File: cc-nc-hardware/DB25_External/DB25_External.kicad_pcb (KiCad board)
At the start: 2 copper layers, 72.2 x 57.7 mm, 88 parts, among them J1 Conn_01x03_Male, J2 DB25_Male_MountingHoles, J4 SW, SW1 SW_MEC_5E, U1 SN74CBTD3384, U2 SN74CBTD3384, U3 AMS1117-2.85, U4 LVT245, U5 LVT125, U6 LVT125, U7 LVT125, U8 74HC14, U9 LVT245

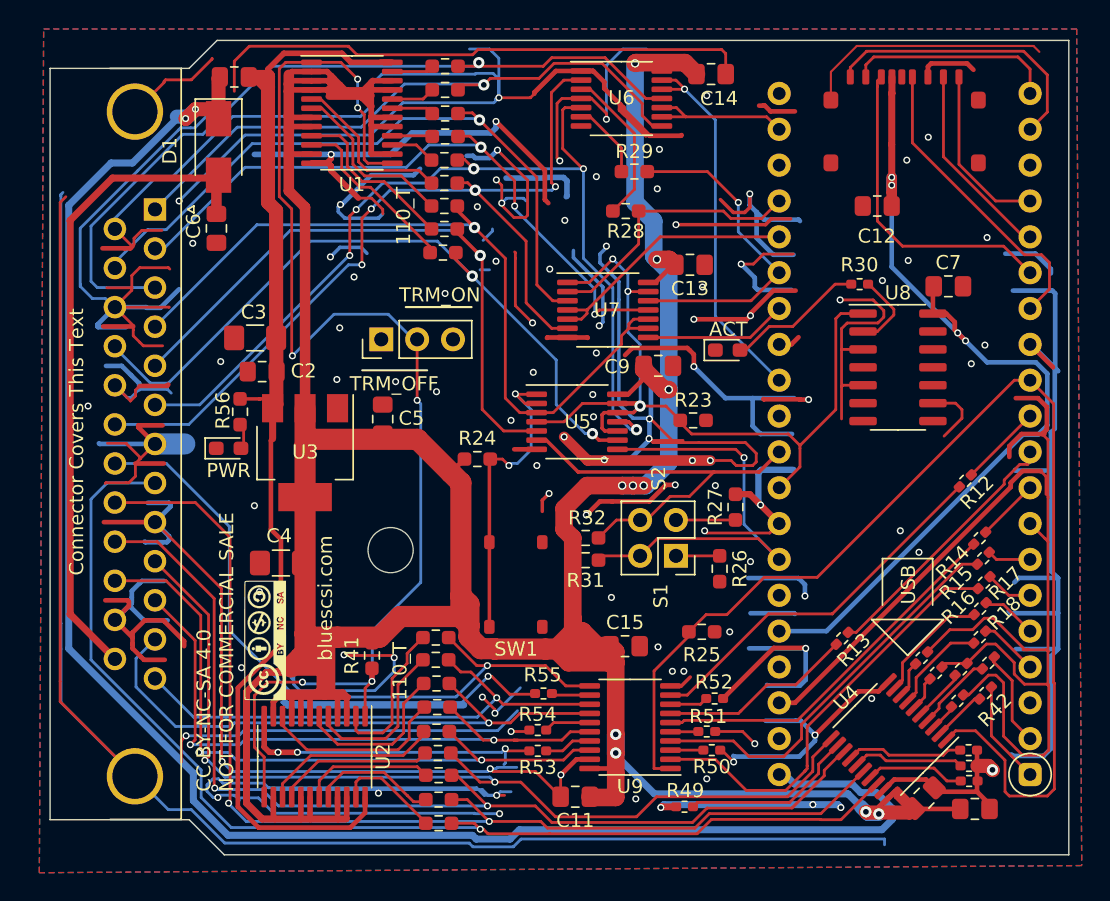
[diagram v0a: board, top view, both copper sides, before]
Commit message: DB25 2023_06a, Smaller Design
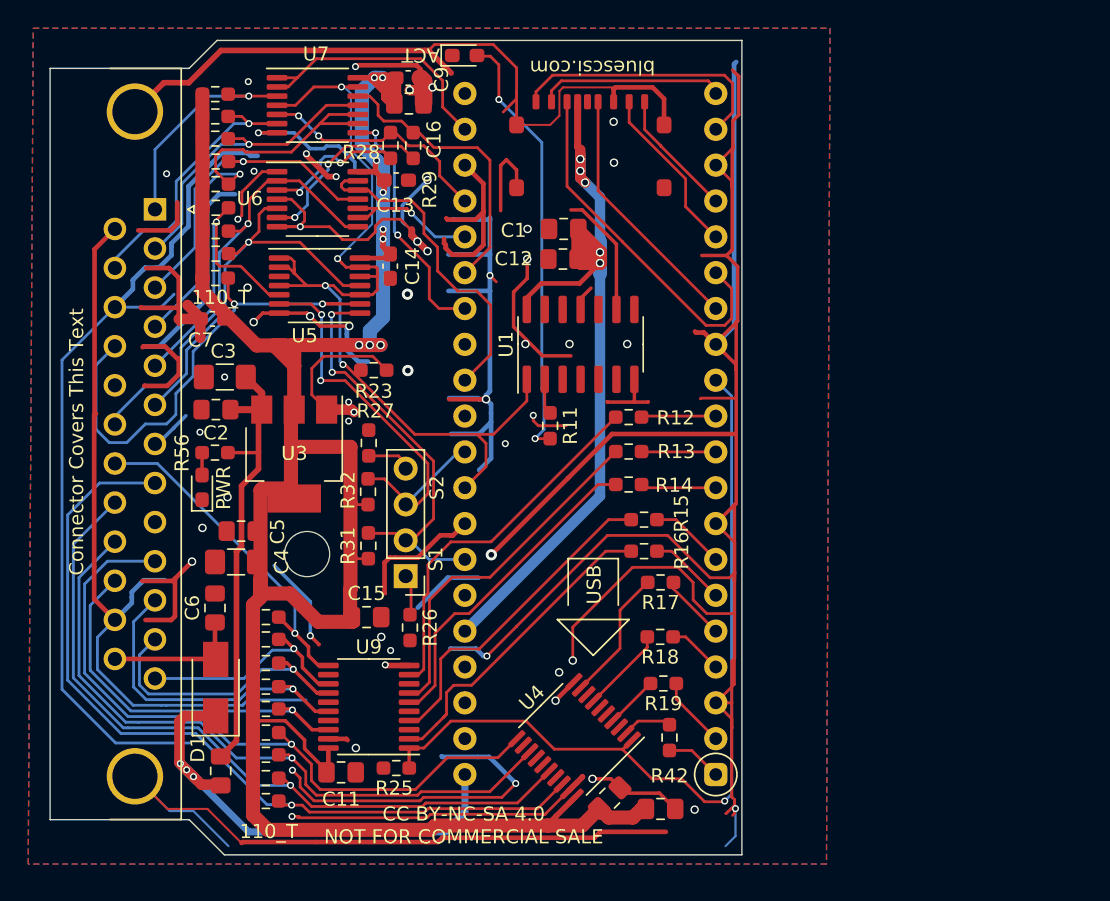
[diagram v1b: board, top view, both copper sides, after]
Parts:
- removed J4: SW, Connector_PinHeader_2.54mm:PinHeader_2x02_P2.54mm_Vertical
- removed R24: 1k, Resistor_SMD:R_0603_1608Metric_Pad0.98x0.95mm_HandSolder
- removed R30: 470, Resistor_SMD:R_0402_1005Metric_Pad0.72x0.64mm_HandSolder
- removed R41: 4.7k, Resistor_SMD:R_0603_1608Metric_Pad0.98x0.95mm_HandSolder
- removed R43, R44, R45, R46, R47, R48, R49, R50, R51, R52, R53, R54, R55: 1k, Resistor_SMD:R_0402_1005Metric_Pad0.72x0.64mm_HandSolder
- removed SW1: SW_MEC_5E, Library:TS-1187A-B-A-B
- removed U2: SN74CBTD3384, Package_SO:TSSOP-24_4.4x7.8mm_P0.65mm
- removed U8: 74HC14, Package_SO:SOIC-14_3.9x8.7mm_P1.27mm
- added C1: 100n, Capacitor_SMD:C_0805_2012Metric_Pad1.18x1.45mm_HandSolder, F.Cu at (136.4, 85.4)
- added C16: 4.7uF, Capacitor_SMD:C_0805_2012Metric_Pad1.18x1.45mm_HandSolder, F.Cu at (125.5, 76.6)
- C13, C14, C9: footprint Capacitor_SMD:C_0805_2012Metric_Pad1.18x1.45mm_HandSolder -> Capacitor_SMD:C_0603_1608Metric_Pad1.08x0.95mm_HandSolder
- C3, C4: value 20uF -> 47uF
- C7: value 4.7uF -> 0.1uF; footprint Capacitor_SMD:C_0805_2012Metric_Pad1.18x1.45mm_HandSolder -> Capacitor_SMD:C_0603_1608Metric_Pad1.08x0.95mm_HandSolder
- G***: moved to B.Cu
- J1: value Conn_01x03_Male -> Conn_01x04_Male; footprint Connector_PinHeader_2.54mm:PinHeader_1x03_P2.54mm_Vertical -> Connector_PinHeader_2.54mm:PinHeader_1x04_P2.54mm_Vertical
- R11: value 1k -> 470; footprint Resistor_SMD:R_0402_1005Metric_Pad0.72x0.64mm_HandSolder -> Resistor_SMD:R_0603_1608Metric_Pad0.98x0.95mm_HandSolder
- R12, R13, R14, R15, R16, R17, R18, R19, R42: footprint Resistor_SMD:R_0402_1005Metric_Pad0.72x0.64mm_HandSolder -> Resistor_SMD:R_0603_1608Metric_Pad0.98x0.95mm_HandSolder
- U1: value SN74CBTD3384 -> 74HC14; footprint Package_SO:TSSOP-24_4.4x7.8mm_P0.65mm -> Package_SO:SOIC-14_3.9x8.7mm_P1.27mm
- moved C7 52.2 mm to (111.5, 91.8), turned to 180 degrees
- moved F2 49.2 mm to (112.1, 123.9), turned to -90 degrees
- moved D1 38.3 mm to (111.8, 118.0), turned to 90 degrees
- moved R11 34.8 mm to (135.5, 99.4), turned to -90 degrees
- moved D2 28.0 mm to (129.4, 73.2)
- moved C9 27.0 mm to (125.4, 74.8)
- moved C6 26.9 mm to (111.7, 112.3), turned to 90 degrees
- moved C14 26.5 mm to (124.1, 88.1), turned to 90 degrees
- moved R27 26.4 mm to (122.6, 100.6)
- moved U7 25.2 mm to (119.0, 76.7)
- moved R14 25.2 mm to (141.0, 103.6), turned to 180 degrees
- moved R12 24.3 mm to (141.0, 98.8), turned to 180 degrees
- moved G*** 24.2 mm to (138.5, 121.5), turned to 180 degrees
- moved R15 24.2 mm to (142.1, 106.0), turned to 180 degrees
- moved R16 24.2 mm to (142.1, 108.3), turned to 180 degrees
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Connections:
- C7 pad 1: +3V3 -> +2V8
- J1 pad 1: unconnected-(J1-Pad1) -> Net-(J1-Pad1)
- J1 pad 2: TRM_ON_J -> iATN
- J1 pad 3: GND -> iACK
- R1 pad 1: Net-(R1-Pad1) -> +2V8
- R10 pad 1: Net-(R10-Pad1) -> +2V8
- R11 pad 1: GND -> Net-(R11-Pad1)
- R11 pad 2: Net-(R11-Pad2) -> Net-(D2-Pad2)
- R2 pad 1: Net-(R2-Pad1) -> +2V8
- R26 pad 1: Net-(J4-Pad1) -> Net-(J1-Pad1)
- R27 pad 1: Net-(J4-Pad3) -> Net-(J1-Pad4)
- R3 pad 1: Net-(R3-Pad1) -> +2V8
- R33 pad 1: Net-(R33-Pad1) -> +2V8
- R34 pad 1: Net-(R34-Pad1) -> +2V8
- R35 pad 1: Net-(R35-Pad1) -> +2V8
- R36 pad 1: Net-(R36-Pad1) -> +2V8
- R37 pad 1: Net-(R37-Pad1) -> +2V8
- R38 pad 1: Net-(R38-Pad1) -> +2V8
- R39 pad 1: Net-(R39-Pad1) -> +2V8
- R4 pad 1: Net-(R4-Pad1) -> +2V8
- R40 pad 1: Net-(R40-Pad1) -> +2V8
- R5 pad 1: Net-(R5-Pad1) -> +2V8
- R6 pad 1: Net-(R6-Pad1) -> +2V8
- R7 pad 1: Net-(R7-Pad1) -> +2V8
- R8 pad 1: Net-(R8-Pad1) -> +2V8
- R9 pad 1: Net-(R9-Pad1) -> +2V8
- U1 pad 1: TRM_ON_J -> oBSY
- U1 pad 10: Net-(R2-Pad1) -> unconnected-(U1-Pad10)
- U1 pad 11: +2V8 -> GND
- U1 pad 12: GND -> unconnected-(U1-Pad12)
- U1 pad 13: TRM_ON_J -> GND
- U1 pad 14: +2V8 -> +3V3
- U1 pad 2: +2V8 -> Net-(R11-Pad1)
- U1 pad 3: +2V8 -> GND
- U1 pad 4: +2V8 -> unconnected-(U1-Pad4)
- U1 pad 5: Net-(R5-Pad1) -> GND
- U1 pad 6: Net-(R4-Pad1) -> unconnected-(U1-Pad6)
- U1 pad 7: +2V8 -> GND
- U1 pad 8: +2V8 -> unconnected-(U1-Pad8)
- U1 pad 9: Net-(R3-Pad1) -> GND
- U4 pad 12: Net-(R49-Pad1) -> unconnected-(U4-Pad12)
- U4 pad 14: Net-(R48-Pad1) -> unconnected-(U4-Pad14)
- U4 pad 15: Net-(R47-Pad1) -> unconnected-(U4-Pad15)
- U4 pad 17: Net-(R46-Pad1) -> unconnected-(U4-Pad17)
- U4 pad 3: Net-(R11-Pad2) -> unconnected-(U4-Pad3)
- U4 pad 5: Net-(R43-Pad2) -> unconnected-(U4-Pad5)
- U4 pad 6: Net-(R44-Pad2) -> unconnected-(U4-Pad6)
- U4 pad 8: Net-(R45-Pad2) -> unconnected-(U4-Pad8)
- U5 pad 1: oRST -> oBSY
- U5 pad 2: oRST -> oBSY
- U5 pad 3: RST -> unconnected-(U5-Pad3)
- U6 pad 10: oREQ -> oSEL
- U6 pad 8: REQ -> SEL
- U6 pad 9: oREQ -> oSEL
- U7 pad 1: oBSY -> oREQ
- U7 pad 2: oCD_iSEL -> oREQ
- U7 pad 3: CD -> REQ
- U7 pad 4: oSEL -> oBSY
- U7 pad 5: oSEL -> oCD_iSEL
- U7 pad 6: SEL -> CD
- U9 pad 12: Net-(R55-Pad1) -> unconnected-(U9-Pad12)
- U9 pad 15: Net-(R54-Pad1) -> unconnected-(U9-Pad15)
- U9 pad 17: Net-(R53-Pad1) -> unconnected-(U9-Pad17)
- U9 pad 3: Net-(R50-Pad2) -> unconnected-(U9-Pad3)
- U9 pad 5: Net-(R51-Pad2) -> unconnected-(U9-Pad5)
- U9 pad 8: Net-(R52-Pad2) -> unconnected-(U9-Pad8)
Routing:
- net GND: track 1137.4 -> 681.1 mm, vias 105 -> 55
- net +2V8: track 334.0 -> 180.2 mm, vias 10 -> 9
- net TRM_ON_J: track 91.9 -> 0.00 mm, vias 6 -> 0
- net +5VP: track 124.6 -> 36.0 mm, vias 2 -> 3
- net +5F: track 80.8 -> 33.2 mm
- net BSY: track 68.8 -> 29.0 mm, vias 5 -> 1
- net +5V: track 47.0 -> 9.80 mm
- net IO: track 57.2 -> 23.1 mm
- net SEL: track 65.3 -> 32.0 mm, vias 4 -> 1
- net CD: track 48.6 -> 19.4 mm
- net REQ: track 44.6 -> 16.0 mm
- net MSG: track 47.7 -> 22.0 mm, vias 3 -> 1
- net DB1: track 78.8 -> 53.2 mm, vias 2 -> 1
- net DBP: track 49.9 -> 24.4 mm
- net DBPTr: track 84.5 -> 59.4 mm, vias 0 -> 1
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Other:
- board size 72.2 x 57.7 mm -> 49 x 57.7 mm
- board text added: "Thanks for looking at the PCB! © 2023 Tech by Androda, LLC Licensed Attribution-NonCommercial-ShareAlike 4.0 International (CC BY-NC-SA 4.0) https://creativecommons.org/licenses/by-nc-sa/4.0/legalcode"
- board text added: "V2 - 2023.06a"
- board text removed: "TRM_OFF"
- board text removed: "TRM_ON"
- board text removed: "V2 - 2022.12a"

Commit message: DB25 Hardware Version 2024.01a, Narrower
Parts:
- removed J1: Conn_01x04_Male, Connector_PinHeader_2.54mm:PinHeader_1x04_P2.54mm_Vertical
- removed R26, R27: 1k, Resistor_SMD:R_0603_1608Metric_Pad0.98x0.95mm_HandSolder
- removed R31, R32: 4.7k, Resistor_SMD:R_0603_1608Metric_Pad0.98x0.95mm_HandSolder
- removed REF**: MountingHole_3.2mm_M3, MountingHole:MountingHole_3.2mm_M3
- G***: moved to F.Cu
- moved G*** 22.7 mm to (124.1, 103.9), turned to 90 degrees
- moved C10 6.38 mm to (137.5, 123.8)
- moved C8 6.38 mm to (133.6, 123.8), turned to 180 degrees
- moved U1 4.31 mm to (136.1, 97.7)
- moved D2 4.11 mm to (132.3, 76.1), turned to -90 degrees
- moved C15 4.09 mm to (119.4, 110.2)
- moved U9 4.03 mm to (122.1, 115.3)
- moved C11 4.01 mm to (120.6, 119.9)
- moved R25 4.01 mm to (124.6, 119.6)
- moved U7 3.36 mm to (118.7, 80.0)
- moved R11 3.34 mm to (134.1, 102.5), turned to 0 degrees
- moved U6 3.20 mm to (119.1, 86.5)
- moved C14 3.09 mm to (124.2, 91.2)
- moved U5 3.05 mm to (119.1, 92.5)
- moved C1 2.95 mm to (136.4, 88.4)
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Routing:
- net GND: track 681.1 -> 864.6 mm, vias 55 -> 75
- net +2V8: track 180.2 -> 161.7 mm
- net iACK: track 31.3 -> 17.8 mm
- net SD_CMD_MOSI: track 25.7 -> 16.6 mm
- net iATN: track 30.1 -> 21.3 mm
- net RST: track 31.8 -> 25.5 mm, vias 1 -> 2
- net oBSY: track 66.9 -> 61.5 mm, vias 4 -> 5
- net DBP: track 24.4 -> 20.3 mm
- net Net-(J1-Pad4): track 3.46 -> 0.00 mm
- net oIO: track 23.4 -> 20.1 mm
- net +5VP: track 36.0 -> 32.8 mm
- net DBPTr: track 59.4 -> 62.4 mm
- net ACK: track 21.8 -> 24.6 mm
- net Net-(D2-A): track 31.0 -> 28.3 mm
- net DB5T: track 23.3 -> 20.5 mm
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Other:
- board size 49 x 57.7 mm -> 49 x 53.2 mm
- board text added: "CC BY-NC-SA 4.0"
- board text added: "CC BY-NC-SA 4.0 NOT FOR COMMERCIAL SALE BlueSCSI © Eric Helgeson PCB © Tech by Androda, LLC"
- board text added: "V2 - 2024.01a"
- board text added: "© 2023 - 2024 Tech by Androda, LLC Licensed Attribution-NonCommercial-ShareAlike 4.0 International (CC BY-NC-SA 4.0) https://creativecommons.org/licenses/by-nc-sa/4.0/legalcode"
- board text removed: "BlueSCSI © Eric Helgeson PCB © Tech by Androda, LLC"
- board text removed: "CC BY-NC-SA 4.0 NOT FOR COMMERCIAL SALE"
- board text removed: "S1"
- board text removed: "S2"
- board text removed: "Thanks for looking at the PCB! © 2023 Tech by Androda, LLC Licensed Attribution-NonCommercial-ShareAlike 4.0 International (CC BY-NC-SA 4.0) https://creativecommons.org/licenses/by-nc-sa/4.0/legalcode"
- board text removed: "V2 - 2023.06a"
